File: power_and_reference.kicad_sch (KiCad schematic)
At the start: 23 parts, among them Q1 ZXTN4004KQTC, U1 BQ79616PAPRQ1

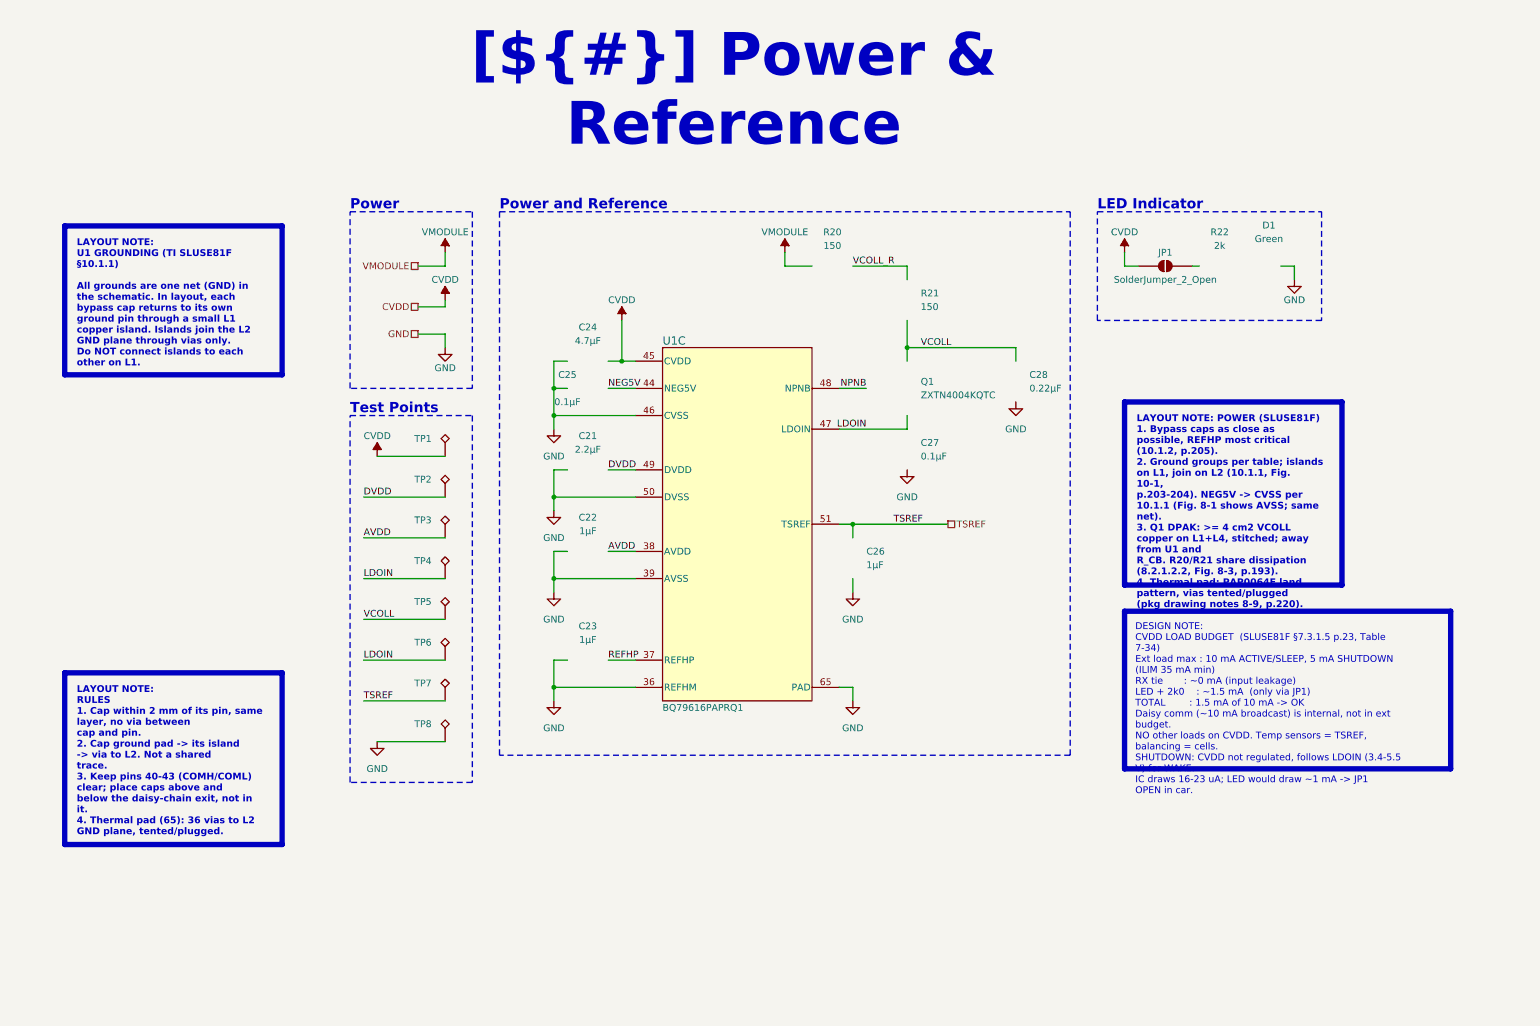
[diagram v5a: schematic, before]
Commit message: PCB[Test Points, Mechanical, Silk]: Finalized Mounting Points, Added Testpoints with adjecent silkscreen labels. SCH[Test Points, Notes]: Added/Updated notes for all pages, cleaned up errors spelling ect.
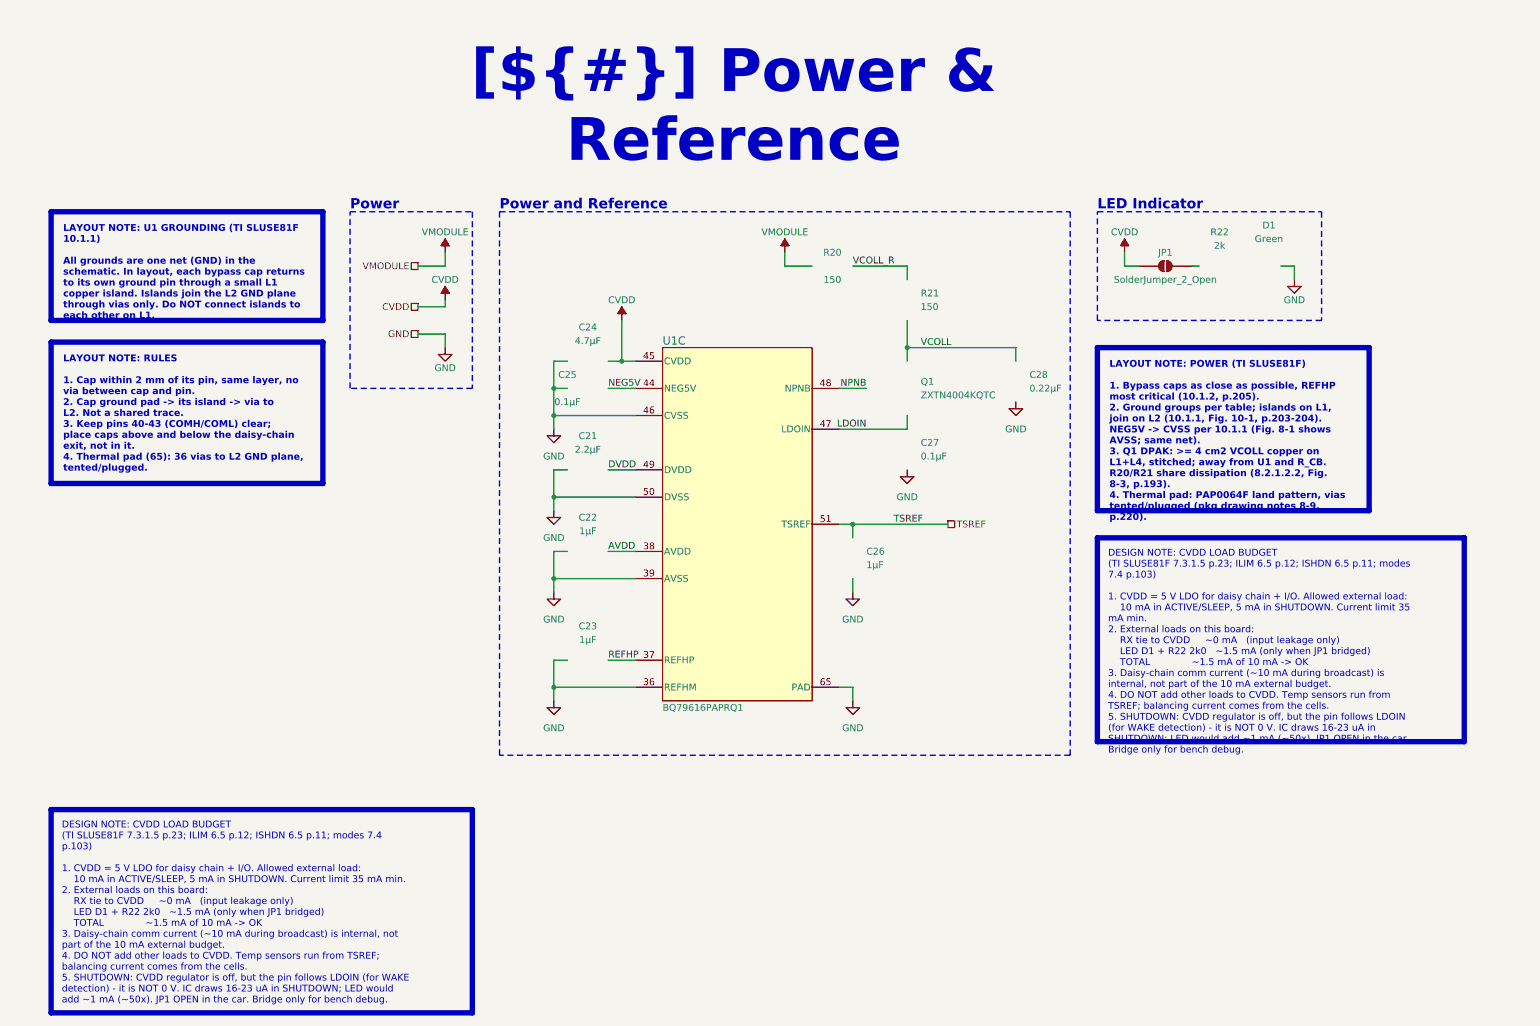
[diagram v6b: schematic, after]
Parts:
- removed TP1, TP2, TP3, TP4, TP5, TP6, TP7, TP8: (no value), TestPoint:TestPoint_Pad_D2.0mm, symbol Connector:TestPoint_Alt
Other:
- note removed: "Test Points"

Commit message: PCB[Trace Size, Testpad, Daisy]: Changed Bat Trace size FAT, Made test pads larger, small trace movement to clean up, daisy trace change. SCH[Notes]: Small notes changes.
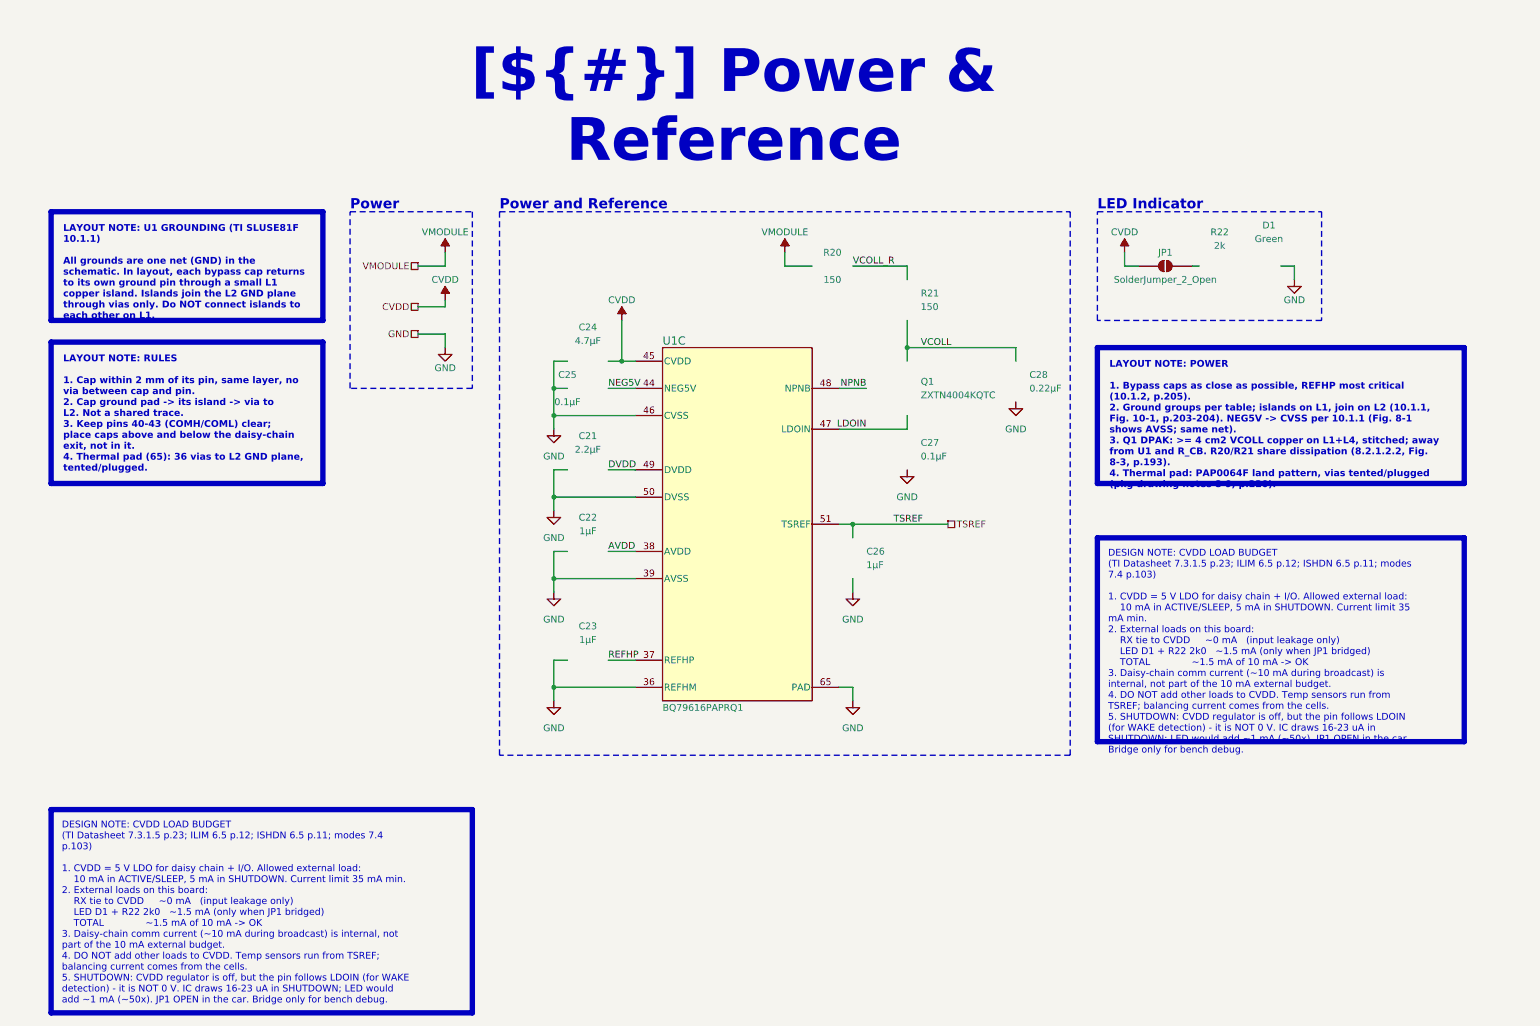
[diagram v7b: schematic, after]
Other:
- company: (none) -> ${COMPANY}
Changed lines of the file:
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@@
 	(title_block
 		(title "Power & Reference")
+		(date "2026-10-28")
+		(rev "${REVISION}")
+		(company "${COMPANY}")
 	)
 	(rectangle
@@
 		)
 	)
-	(text_box "LAYOUT NOTE: POWER (TI SLUSE81F)\n\n1. Bypass caps as close as possible, REFHP most critical (10.1.2, p.205).\n2. Ground groups per table; islands on L1, join on L2 (10.1.1, Fig. 10-1, p.203-204). NEG5V -> CVSS per 10.1.1 (Fig. 8-1 shows AVSS; same net).\n3. Q1 DPAK: >= 4 cm2 VCOLL copper on L1+L4, stitched; away from U1 and R_CB. R20/R21 share dissipation (8.2.1.2.2, Fig. 8-3, p.193).\n4. Thermal pad: PAP0064F land pattern, vias tented/plugged (pkg drawing notes 8-9, p.220)."
+	(text_box "LAYOUT NOTE: POWER\n\n1. Bypass caps as close as possible, REFHP most critical (10.1.2, p.205).\n2. Ground groups per table; islands on L1, join on L2 (10.1.1, Fig. 10-1, p.203-204). NEG5V -> CVSS per 10.1.1 (Fig. 8-1 shows AVSS; same net).\n3. Q1 DPAK: >= 4 cm2 VCOLL copper on L1+L4, stitched; away from U1 and R_CB. R20/R21 share dissipation (8.2.1.2.2, Fig. 8-3, p.193).\n4. Thermal pad: PAP0064F land pattern, vias tented/plugged (pkg drawing notes 8-9, p.220)."
 		(exclude_from_sim no)
 		(at 210.82 71.12 0)
-		(size 50.8 30.48)
+		(size 68.58 25.4)
 		(margins 2.25 2.25 2.25 2.25)
 		(stroke
@@
 		)
 	)
-	(text_box "DESIGN NOTE: CVDD LOAD BUDGET\n(TI SLUSE81F 7.3.1.5 p.23; ILIM 6.5 p.12; ISHDN 6.5 p.11; modes 7.4 p.103)\n\n1. CVDD = 5 V LDO for daisy chain + I/O. Allowed external load:\n	10 mA in ACTIVE/SLEEP, 5 mA in SHUTDOWN. Current limit 35 mA min.\n2. External loads on this board:\n	RX tie to CVDD     ~0 mA   (input leakage only)\n	LED D1 + R22 2k0   ~1.5 mA (only when JP1 bridged)\n	TOTAL              ~1.5 mA of 10 mA -> OK\n3. Daisy-chain comm current (~10 mA during broadcast) is internal, not part of the 10 mA external budget.\n4. DO NOT add other loads to CVDD. Temp sensors run from TSREF; balancing current comes from the cells.\n5. SHUTDOWN: CVDD regulator is off, but the pin follows LDOIN (for WAKE detection) - it is NOT 0 V. IC draws 16-23 uA in SHUTDOWN; LED would add ~1 mA (~50x). JP1 OPEN in the car. Bridge only for bench debug."
+	(text_box "DESIGN NOTE: CVDD LOAD BUDGET\n(TI Datasheet 7.3.1.5 p.23; ILIM 6.5 p.12; ISHDN 6.5 p.11; modes 7.4 p.103)\n\n1. CVDD = 5 V LDO for daisy chain + I/O. Allowed external load:\n	10 mA in ACTIVE/SLEEP, 5 mA in SHUTDOWN. Current limit 35 mA min.\n2. External loads on this board:\n	RX tie to CVDD     ~0 mA   (input leakage only)\n	LED D1 + R22 2k0   ~1.5 mA (only when JP1 bridged)\n	TOTAL              ~1.5 mA of 10 mA -> OK\n3. Daisy-chain comm current (~10 mA during broadcast) is internal, not part of the 10 mA external budget.\n4. DO NOT add other loads to CVDD. Temp sensors run from TSREF; balancing current comes from the cells.\n5. SHUTDOWN: CVDD regulator is off, but the pin follows LDOIN (for WAKE detection) - it is NOT 0 V. IC draws 16-23 uA in SHUTDOWN; LED would add ~1 mA (~50x). JP1 OPEN in the car. Bridge only for bench debug."
 		(exclude_from_sim no)
 		(at 15.24 157.48 0)
@@
 		)
 	)
-	(text_box "DESIGN NOTE: CVDD LOAD BUDGET\n(TI SLUSE81F 7.3.1.5 p.23; ILIM 6.5 p.12; ISHDN 6.5 p.11; modes 7.4 p.103)\n\n1. CVDD = 5 V LDO for daisy chain + I/O. Allowed external load:\n	10 mA in ACTIVE/SLEEP, 5 mA in SHUTDOWN. Current limit 35 mA min.\n2. External loads on this board:\n	RX tie to CVDD     ~0 mA   (input leakage only)\n	LED D1 + R22 2k0   ~1.5 mA (only when JP1 bridged)\n	TOTAL              ~1.5 mA of 10 mA -> OK\n3. Daisy-chain comm current (~10 mA during broadcast) is internal, not part of the 10 mA external budget.\n4. DO NOT add other loads to CVDD. Temp sensors run from TSREF; balancing current comes from the cells.\n5. SHUTDOWN: CVDD regulator is off, but the pin follows LDOIN (for WAKE detection) - it is NOT 0 V. IC draws 16-23 uA in SHUTDOWN; LED would add ~1 mA (~50x). JP1 OPEN in the car. Bridge only for bench debug."
+	(text_box "DESIGN NOTE: CVDD LOAD BUDGET\n(TI Datasheet 7.3.1.5 p.23; ILIM 6.5 p.12; ISHDN 6.5 p.11; modes 7.4 p.103)\n\n1. CVDD = 5 V LDO for daisy chain + I/O. Allowed external load:\n	10 mA in ACTIVE/SLEEP, 5 mA in SHUTDOWN. Current limit 35 mA min.\n2. External loads on this board:\n	RX tie to CVDD     ~0 mA   (input leakage only)\n	LED D1 + R22 2k0   ~1.5 mA (only when JP1 bridged)\n	TOTAL              ~1.5 mA of 10 mA -> OK\n3. Daisy-chain comm current (~10 mA during broadcast) is internal, not part of the 10 mA external budget.\n4. DO NOT add other loads to CVDD. Temp sensors run from TSREF; balancing current comes from the cells.\n5. SHUTDOWN: CVDD regulator is off, but the pin follows LDOIN (for WAKE detection) - it is NOT 0 V. IC draws 16-23 uA in SHUTDOWN; LED would add ~1 mA (~50x). JP1 OPEN in the car. Bridge only for bench debug."
 		(exclude_from_sim no)
 		(at 210.82 106.68 0)
